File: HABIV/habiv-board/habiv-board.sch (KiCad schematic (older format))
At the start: 84 parts, among them IC1 RTC_PCF8523T, J1 Conn_01x11_Male, J10 Conn_01x02_Male, J11 Conn_02x01, J12 Conn_01x02_Male, J13 Conn_01x02_Male, J14 Conn_01x08_Male, J15 Conn_01x03_Male, J16 Conn_01x04_Male, J17 Conn_01x05_Male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

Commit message: some habiv schematic changes
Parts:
- removed J1: Conn_01x11_Male, Pin_Headers:Pin_Header_Straight_1x11_Pitch2.54mm, symbol habiv-board-rescue:Conn_01x11_Male-STM32-rescue
- added C? (x2): C_Small, symbol Device:C_Small
- added R? (x2): 8.2k, symbol Device:R_Small
- added R? (x5): 56k, symbol Device:R_Small
- added U?: LSM9DS1TR, digikey-footprints:LGA-24_3x3.5mm_LSM9DS1, symbol dk_Motion-Sensors-IMUs-Inertial-Measurement-Units:LSM9DS1TR
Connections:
- wire segments 344 -> 355
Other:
- moved on the sheet: B1, C1, C11, C12, C13, C14, C2, C8, C9, D3, D4, IC1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

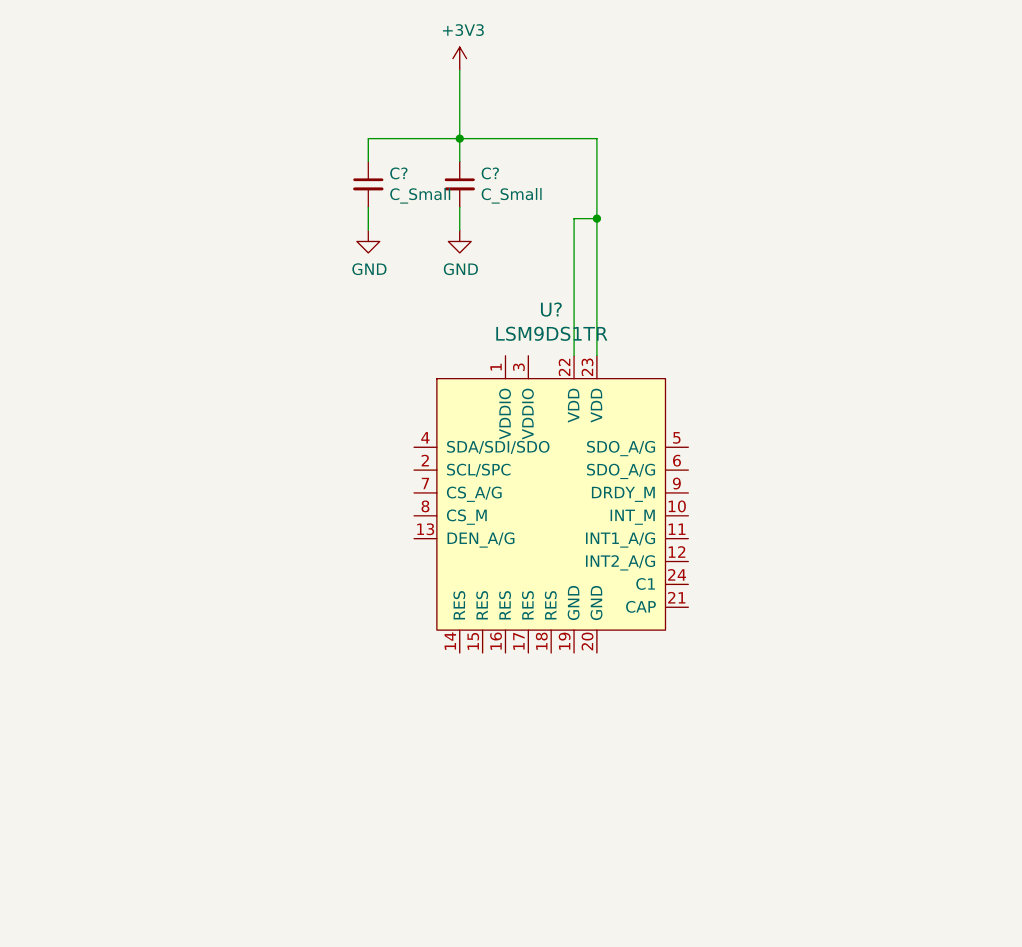
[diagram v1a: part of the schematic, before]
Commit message: implemented IMU power and ground connection with decoupling caps
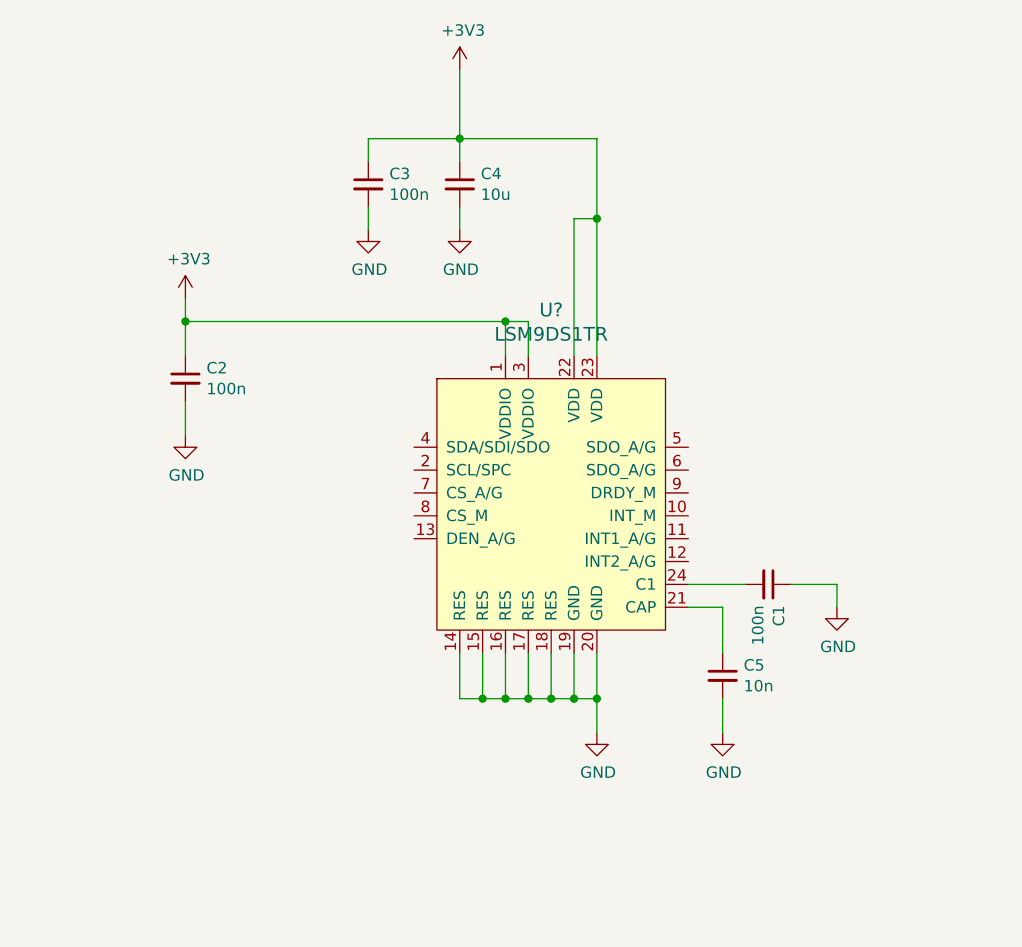
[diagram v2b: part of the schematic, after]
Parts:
- added C1, C2: 100n, symbol Device:C_Small
- added C5: 10n, symbol Device:C_Small
- C3: renamed from C?; value C_Small -> 100n
- C4: renamed from C?; value C_Small -> 10u
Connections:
- wire segments 355 -> 382
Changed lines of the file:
@@
 	17450 8750 17450 9050
 $Comp
-L Device:C_Small C?
+L Device:C_Small C4
 U 1 1 5CE00EC9
 P 17450 9250
-F 0 "C?" H 17542 9296 50  0000 L CNN
-F 1 "C_Small" H 17542 9205 50  0000 L CNN
+F 0 "C4" H 17542 9296 50  0000 L CNN
+F 1 "10u" H 17542 9205 50  0000 L CNN
 F 2 "" H 17450 9250 50  0001 C CNN
 F 3 "~" H 17450 9250 50  0001 C CNN
@@
 $EndComp
 $Comp
-L Device:C_Small C?
+L Device:C_Small C3
 U 1 1 5CEDE690
 P 17050 9250
-F 0 "C?" H 17142 9296 50  0000 L CNN
-F 1 "C_Small" H 17142 9205 50  0000 L CNN
+F 0 "C3" H 17142 9296 50  0000 L CNN
+F 1 "100n" H 17142 9205 50  0000 L CNN
 F 2 "" H 17050 9250 50  0001 C CNN
 F 3 "~" H 17050 9250 50  0001 C CNN
@@
 	1    0    0    -1
 $EndComp
+$Comp
+L Device:C_Small C5
+U 1 1 5C7D1725
+P 18600 11400
+F 0 "C5" H 18692 11446 50  0000 L CNN
+F 1 "10n" H 18692 11355 50  0000 L CNN
+F 2 "" H 18600 11400 50  0001 C CNN
+F 3 "~" H 18600 11400 50  0001 C CNN
+	1    18600 11400
+	1    0    0    -1
+$EndComp
+$Comp
+L Device:C_Small C2
+U 1 1 5C7D1829
+P 16250 10100
+F 0 "C2" H 16342 10146 50  0000 L CNN
+F 1 "100n" H 16342 10055 50  0000 L CNN
+F 2 "" H 16250 10100 50  0001 C CNN
+F 3 "~" H 16250 10100 50  0001 C CNN
+	1    16250 10100
+	1    0    0    -1
+$EndComp
+$Comp
+L Device:C_Small C1
+U 1 1 5C7D291A
+P 18800 11000
+F 0 "C1" H 18892 11046 50  0000 L CNN
+F 1 "100n" H 18892 10955 50  0000 L CNN
+F 2 "" H 18800 11000 50  0001 C CNN
+F 3 "~" H 18800 11000 50  0001 C CNN
+	1    18800 11000
+	0    1    1    0
+$EndComp
+Wire Wire Line
+	18700 11000 18450 11000
+Wire Wire Line
+	18450 11100 18600 11100
+Wire Wire Line
+	18600 11100 18600 11300
+$Comp
+L power:GND #PWR?
+U 1 1 5C85493C
+P 19100 11100
+F 0 "#PWR?" H 19100 10850 50  0001 C CNN
+F 1 "GND" H 19105 10927 50  0000 C CNN
+F 2 "" H 19100 11100 50  0001 C CNN
+F 3 "" H 19100 11100 50  0001 C CNN
+	1    19100 11100
+	1    0    0    -1
+$EndComp
+$Comp
+L power:GND #PWR?
+U 1 1 5C854A0C
+P 18600 11650
+F 0 "#PWR?" H 18600 11400 50  0001 C CNN
+F 1 "GND" H 18605 11477 50  0000 C CNN
+F 2 "" H 18600 11650 50  0001 C CNN
+F 3 "" H 18600 11650 50  0001 C CNN
+	1    18600 11650
+	1    0    0    -1
+$EndComp
+Wire Wire Line
+	18600 11500 18600 11650
+Wire Wire Line
+	19100 11100 19100 11000
+Wire Wire Line
+	19100 11000 18900 11000
+Wire Wire Line
+	17450 11300 17450 11500
+Wire Wire Line
+	17450 11500 17550 11500
+Wire Wire Line
+	17550 11500 17550 11300
+Wire Wire Line
+	17550 11500 17650 11500
+Wire Wire Line
+	17650 11500 17650 11300
+Connection ~ 17550 11500
+Wire Wire Line
+	17750 11300 17750 11500
+Wire Wire Line
+	17750 11500 17650 11500
+Connection ~ 17650 11500
+Wire Wire Line
+	17850 11300 17850 11500
+Wire Wire Line
+	17850 11500 17750 11500
+Connection ~ 17750 11500
+Wire Wire Line
+	17950 11300 17950 11500
+Wire Wire Line
+	17950 11500 17850 11500
+Connection ~ 17850 11500
+Wire Wire Line
+	18050 11300 18050 11500
+Wire Wire Line
+	18050 11500 17950 11500
+Connection ~ 17950 11500
+$Comp
+L power:GND #PWR?
+U 1 1 5C963F0A
+P 18050 11650
+F 0 "#PWR?" H 18050 11400 50  0001 C CNN
+F 1 "GND" H 18055 11477 50  0000 C CNN
+F 2 "" H 18050 11650 50  0001 C CNN
+F 3 "" H 18050 11650 50  0001 C CNN
+	1    18050 11650
+	1    0    0    -1
+$EndComp
+Wire Wire Line
+	18050 11500 18050 11650
+Connection ~ 18050 11500
+Wire Wire Line
+	17650 10000 17650 9850
+Wire Wire Line
+	17650 9850 17750 9850
+Wire Wire Line
+	17750 9850 17750 10000
+Wire Wire Line
+	17650 9850 16250 9850
+Wire Wire Line
+	16250 9850 16250 10000
+Connection ~ 17650 9850
+$Comp
+L power:GND #PWR?
+U 1 1 5C9CF645
+P 16250 10350
+F 0 "#PWR?" H 16250 10100 50  0001 C CNN
+F 1 "GND" H 16255 10177 50  0000 C CNN
+F 2 "" H 16250 10350 50  0001 C CNN
+F 3 "" H 16250 10350 50  0001 C CNN
+	1    16250 10350
+	1    0    0    -1
+$EndComp
+Wire Wire Line
+	16250 10200 16250 10350
+$Comp
+L power:+3V3 #PWR?
+U 1 1 5C9F3C2A
+P 16250 9750
+F 0 "#PWR?" H 16250 9600 50  0001 C CNN
+F 1 "+3V3" H 16265 9923 50  0000 C CNN
+F 2 "" H 16250 9750 50  0001 C CNN
+F 3 "" H 16250 9750 50  0001 C CNN
+	1    16250 9750
+	1    0    0    -1
+$EndComp
+Wire Wire Line
+	16250 9750 16250 9850
+Connection ~ 16250 9850
 $EndSCHEMATC

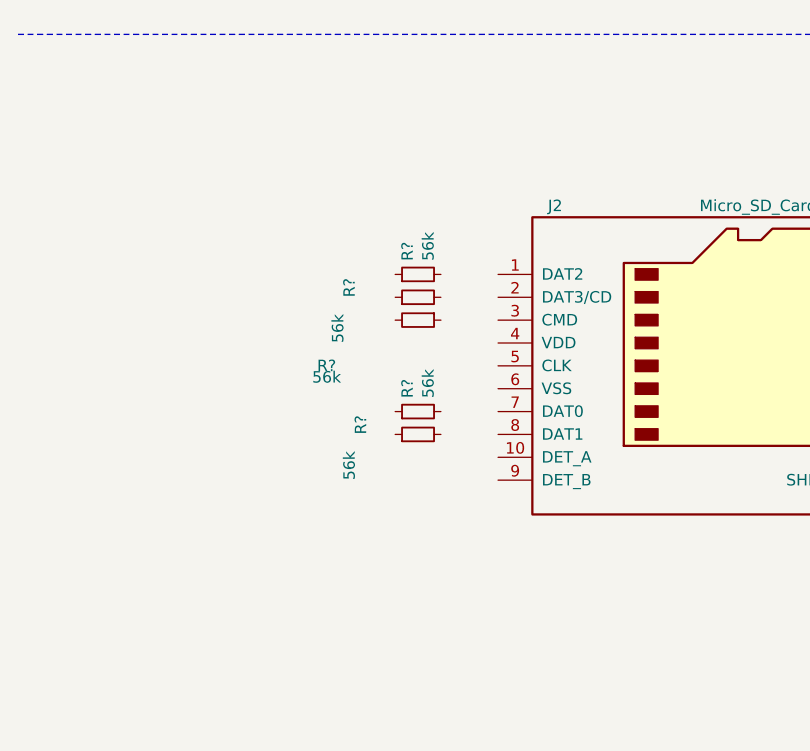
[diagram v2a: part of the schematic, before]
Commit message: SD Card connections
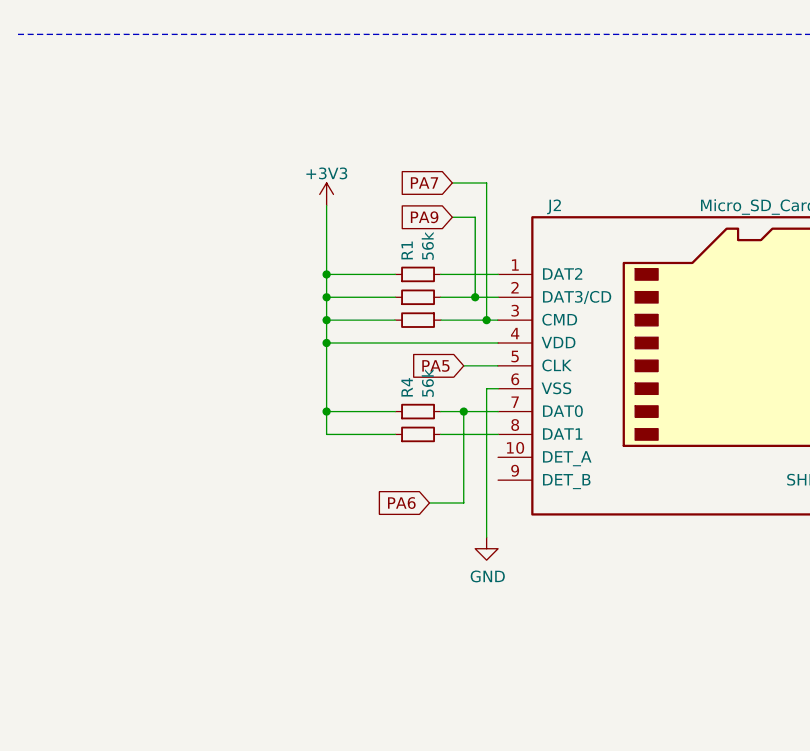
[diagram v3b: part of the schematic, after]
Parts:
- gave numbers to parts that had none: 5
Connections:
- wire segments 382 -> 411
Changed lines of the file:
@@
 	4300 15100 4300 15250
 $Comp
-L Device:R_Small R?
+L Device:R_Small R1
 U 1 1 5CBEDA09
 P 2250 14200
-F 0 "R?" H 2309 14246 50  0000 L CNN
+F 0 "R1" H 2309 14246 50  0000 L CNN
 F 1 "56k" H 2309 14155 50  0000 L CNN
 F 2 "" H 2250 14200 50  0001 C CNN
@@
 $EndComp
 $Comp
-L Device:R_Small R?
+L Device:R_Small R2
 U 1 1 5CCA87E6
 P 2250 14300
-F 0 "R?" H 2250 14600 50  0000 L CNN
-F 1 "56k" H 2050 14650 50  0000 L CNN
+F 0 "R2" H 2250 14600 50  0001 L CNN
+F 1 "56k" H 2050 14650 50  0001 L CNN
 F 2 "" H 2250 14300 50  0001 C CNN
 F 3 "~" H 2250 14300 50  0001 C CNN
@@
 $EndComp
 $Comp
-L Device:R_Small R?
+L Device:R_Small R4
 U 1 1 5CCE56CA
 P 2250 14800
-F 0 "R?" H 2309 14846 50  0000 L CNN
+F 0 "R4" H 2309 14846 50  0000 L CNN
 F 1 "56k" H 2309 14755 50  0000 L CNN
 F 2 "" H 2250 14800 50  0001 C CNN
@@
 $EndComp
 $Comp
-L Device:R_Small R?
+L Device:R_Small R5
 U 1 1 5CD03D14
 P 2250 14900
-F 0 "R?" H 2250 15150 50  0000 L CNN
-F 1 "56k" H 2050 15200 50  0000 L CNN
+F 0 "R5" H 2250 15150 50  0001 L CNN
+F 1 "56k" H 2050 15200 50  0001 L CNN
 F 2 "" H 2250 14900 50  0001 C CNN
 F 3 "~" H 2250 14900 50  0001 C CNN
@@
 $EndComp
 $Comp
-L Device:R_Small R?
+L Device:R_Small R3
 U 1 1 5CD2271E
 P 2250 14400
-F 0 "R?" V 2450 14000 50  0000 C CNN
-F 1 "56k" V 2500 14000 50  0000 C CNN
+F 0 "R3" V 2450 14000 50  0001 C CNN
+F 1 "56k" V 2500 14000 50  0001 C CNN
 F 2 "" H 2250 14400 50  0001 C CNN
 F 3 "~" H 2250 14400 50  0001 C CNN
@@
 	16250 9750 16250 9850
 Connection ~ 16250 9850
+$Comp
+L power:+3V3 #PWR?
+U 1 1 5CA19B2F
+P 1850 13900
+F 0 "#PWR?" H 1850 13750 50  0001 C CNN
+F 1 "+3V3" H 1850 14040 50  0000 C CNN
+F 2 "" H 1850 13900 50  0001 C CNN
+F 3 "" H 1850 13900 50  0001 C CNN
+	1    1850 13900
+	1    0    0    -1
+$EndComp
+Wire Wire Line
+	2150 14200 1850 14200
+Wire Wire Line
+	1850 14200 1850 13900
+Wire Wire Line
+	2350 14200 2600 14200
+Wire Wire Line
+	2350 14300 2500 14300
+Wire Wire Line
+	2150 14300 1850 14300
+Wire Wire Line
+	1850 14300 1850 14200
+Connection ~ 1850 14200
+Wire Wire Line
+	2350 14400 2550 14400
+Wire Wire Line
+	2150 14400 1850 14400
+Wire Wire Line
+	1850 14400 1850 14300
+Connection ~ 1850 14300
+Wire Wire Line
+	2600 14500 1850 14500
+Wire Wire Line
+	1850 14500 1850 14400
+Connection ~ 1850 14400
+Wire Wire Line
+	2150 14800 1850 14800
+Wire Wire Line
+	1850 14800 1850 14500
+Connection ~ 1850 14500
+Wire Wire Line
+	2350 14800 2450 14800
+Wire Wire Line
+	2150 14900 1850 14900
+Wire Wire Line
+	1850 14900 1850 14800
+Connection ~ 1850 14800
+Wire Wire Line
+	2350 14900 2600 14900
+Text GLabel 2300 15200 0    50   Input ~ 0
+PA6
+Wire Wire Line
+	2300 15200 2450 15200
+Wire Wire Line
+	2450 15200 2450 14800
+Connection ~ 2450 14800
+Wire Wire Line
+	2450 14800 2600 14800
+$Comp
+L power:GND #PWR?
+U 1 1 5CC89801
+P 2550 15350
+F 0 "#PWR?" H 2550 15100 50  0001 C CNN
+F 1 "GND" H 2555 15177 50  0000 C CNN
+F 2 "" H 2550 15350 50  0001 C CNN
+F 3 "" H 2550 15350 50  0001 C CNN
+	1    2550 15350
+	1    0    0    -1
+$EndComp
+Wire Wire Line
+	2600 14700 2550 14700
+Wire Wire Line
+	2550 14700 2550 15350
+Text GLabel 2450 14600 0    50   Input ~ 0
+PA5
+Wire Wire Line
+	2450 14600 2600 14600
+Text GLabel 2400 13950 0    50   Input ~ 0
+PA9
+Connection ~ 2500 14300
+Wire Wire Line
+	2500 14300 2600 14300
+Text GLabel 2400 13800 0    50   Input ~ 0
+PA7
+Wire Wire Line
+	2400 13800 2550 13800
+Wire Wire Line
+	2550 13800 2550 14400
+Connection ~ 2550 14400
+Wire Wire Line
+	2550 14400 2600 14400
+Wire Wire Line
+	2400 13950 2500 13950
+Wire Wire Line
+	2500 13950 2500 14300
 $EndSCHEMATC

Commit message: implemented 0 ohm resistors on Vdd pins of ICs, continue to implement 0 ohms on SPI and I2C pin
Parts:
- added R0 (x8), R? (x14): 0, symbol Device:R
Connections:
- wire segments 411 -> 424
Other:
- moved on the sheet: 100nF2, 1uF2

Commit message: finished implementing 0 ohm resistors on clock pins
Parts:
- added R? (x5): 0, symbol Device:R
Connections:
- wire segments 424 -> 427
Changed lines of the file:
@@
 	10300 2150 10400 2150
 Wire Wire Line
-	10500 2450 10500 1950
+	10500 2450 10500 2300
 Wire Wire Line
 	10500 1950 10300 1950
@@
 	12100 2800 12100 2650
 Wire Wire Line
-	10400 2150 10400 2800
+	10400 2150 10400 2250
 Wire Wire Line
 	13050 14850 12350 14850
@@
 	10300 3000 10550 3000
 Wire Wire Line
-	10300 2350 10300 3000
+	10300 2350 10300 2550
 Text GLabel 10550 3000 2    50   Input ~ 0
 PC7
@@
 Text GLabel 19100 1650 2    50   Input ~ 0
 PA8
-Wire Wire Line
-	2450 3300 2200 3300
 Wire Wire Line
 	1500 3000 1600 3000
@@
 $EndComp
 Wire Wire Line
-	1750 3250 2250 3250
-Wire Wire Line
-	2450 3200 2250 3200
-Wire Wire Line
-	2250 3200 2250 3250
+	1750 3250 2100 3250
 Wire Wire Line
 	2450 3100 2050 3100
@@
 Wire Wire Line
 	1500 2200 1500 2450
-Wire Wire Line
-	2250 3200 2100 3200
-Connection ~ 2250 3200
-Text GLabel 2100 3200 0    50   Input ~ 0
+Text GLabel 2000 3200 0    50   Input ~ 0
 PB8
-Text GLabel 2000 3400 0    50   Input ~ 0
+Text GLabel 1950 3400 0    50   Input ~ 0
 PB9
-Wire Wire Line
-	2000 3400 2200 3400
-Wire Wire Line
-	2200 3400 2200 3300
-Connection ~ 2200 3300
-Wire Wire Line
-	2200 3300 1600 3300
 $Comp
 L power:GND #PWR?
@@
 Wire Wire Line
 	2550 14250 2550 14400
+Wire Wire Line
+	2000 3200 2100 3200
+Wire Wire Line
+	2100 3200 2100 3250
+Connection ~ 2100 3200
+Wire Wire Line
+	2100 3200 2150 3200
+Wire Wire Line
+	1950 3400 2100 3400
+Wire Wire Line
+	2100 3400 2100 3300
+Connection ~ 2100 3300
+Wire Wire Line
+	2100 3300 1600 3300
+Wire Wire Line
+	2100 3300 2150 3300
+$Comp
+L Device:R R?
+U 1 1 5D6F92C2
+P 2300 3300
+F 0 "R?" H 2370 3346 50  0000 L CNN
+F 1 "0" V 2300 3250 50  0000 L CNN
+F 2 "" V 2230 3300 50  0001 C CNN
+F 3 "~" H 2300 3300 50  0001 C CNN
+	1    2300 3300
+	0    1    1    0
+$EndComp
+$Comp
+L Device:R R?
+U 1 1 5D6F9447
+P 2300 3200
+F 0 "R?" H 2370 3246 50  0000 L CNN
+F 1 "0" V 2300 3150 50  0000 L CNN
+F 2 "" V 2230 3200 50  0001 C CNN
+F 3 "~" H 2300 3200 50  0001 C CNN
+	1    2300 3200
+	0    1    1    0
+$EndComp
+$Comp
+L Device:R R?
+U 1 1 5D6FA677
+P 10500 2150
+F 0 "R?" H 10570 2196 50  0000 L CNN
+F 1 "0" V 10500 2100 50  0000 L CNN
+F 2 "" V 10430 2150 50  0001 C CNN
+F 3 "~" H 10500 2150 50  0001 C CNN
+	1    10500 2150
+	1    0    0    -1
+$EndComp
+Wire Wire Line
+	10500 2000 10500 1950
+$Comp
+L Device:R R?
+U 1 1 5D6FA78C
+P 10400 2400
+F 0 "R?" H 10470 2446 50  0000 L CNN
+F 1 "0" V 10400 2350 50  0000 L CNN
+F 2 "" V 10330 2400 50  0001 C CNN
+F 3 "~" H 10400 2400 50  0001 C CNN
+	1    10400 2400
+	1    0    0    -1
+$EndComp
+Wire Wire Line
+	10400 2550 10400 2800
+$Comp
+L Device:R R?
+U 1 1 5D6FA891
+P 10300 2700
+F 0 "R?" H 10370 2746 50  0000 L CNN
+F 1 "0" V 10300 2650 50  0000 L CNN
+F 2 "" V 10230 2700 50  0001 C CNN
+F 3 "~" H 10300 2700 50  0001 C CNN
+	1    10300 2700
+	1    0    0    -1
+$EndComp
+Wire Wire Line
+	10300 2850 10300 3000
 $EndSCHEMATC

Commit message: IMU SDA and SCL pins connected to MCU
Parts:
- added R? (x2): 0, symbol Device:R
- added R? (x2): 1K, Resistor_SMD:R_0402_1005Metric, symbol habiv-board-rescue:RESISTOR0805_NOOUTLINE-real_time_clock-eagle-import
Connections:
- wire segments 427 -> 436
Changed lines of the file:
@@
 Wire Wire Line
 	1600 3000 1750 3000
-Connection ~ 1600 3300
 Connection ~ 1750 3000
 Wire Wire Line
@@
 Wire Wire Line
 	1750 3250 2100 3250
-Wire Wire Line
-	2450 3100 2050 3100
-Wire Wire Line
-	1500 3300 1600 3300
 Wire Wire Line
 	1500 2200 2850 2200
@@
 	17750 9850 17750 10000
 Wire Wire Line
-	17650 9850 16250 9850
+	17650 9850 16900 9850
 Wire Wire Line
 	16250 9850 16250 10000
@@
 Wire Wire Line
 	10300 2850 10300 3000
+Text GLabel 16750 10500 0    50   Input ~ 0
+PB8
+Text GLabel 16750 10400 0    50   Input ~ 0
+PB9
+$Comp
+L Device:R R?
+U 1 1 5D897265
+P 17050 10400
+F 0 "R?" H 17120 10446 50  0000 L CNN
+F 1 "0" V 17050 10350 50  0000 L CNN
+F 2 "" V 16980 10400 50  0001 C CNN
+F 3 "~" H 17050 10400 50  0001 C CNN
+	1    17050 10400
+	0    1    1    0
+$EndComp
+Wire Wire Line
+	17200 10400 17250 10400
+$Comp
+L Device:R R?
+U 1 1 5D8973FE
+P 17050 10500
+F 0 "R?" H 17120 10546 50  0000 L CNN
+F 1 "0" V 17050 10450 50  0000 L CNN
+F 2 "" V 16980 10500 50  0001 C CNN
+F 3 "~" H 17050 10500 50  0001 C CNN
+	1    17050 10500
+	0    1    1    0
+$EndComp
+Wire Wire Line
+	17200 10500 17250 10500
+$Comp
+L habiv-board-rescue:RESISTOR0805_NOOUTLINE-real_time_clock-eagle-import R?
+U 1 0 5D898CF1
+P 16900 10100
+F 0 "R?" H 16900 10200 50  0000 C CNN
+F 1 "1K" H 16900 10100 40  0000 C CNB
+F 2 "Resistor_SMD:R_0402_1005Metric" H 16900 10100 50  0001 C CNN
+F 3 "" H 16900 10100 50  0001 C CNN
+	1    16900 10100
+	0    1    1    0
+$EndComp
+$Comp
+L habiv-board-rescue:RESISTOR0805_NOOUTLINE-real_time_clock-eagle-import R?
+U 1 0 5D89AC27
+P 16800 10100
+F 0 "R?" H 16800 10200 50  0000 C CNN
+F 1 "1K" H 16800 10100 40  0000 C CNB
+F 2 "Resistor_SMD:R_0402_1005Metric" H 16800 10100 50  0001 C CNN
+F 3 "" H 16800 10100 50  0001 C CNN
+	1    16800 10100
+	0    1    1    0
+$EndComp
+Wire Wire Line
+	16750 10500 16800 10500
+Wire Wire Line
+	16750 10400 16900 10400
+Wire Wire Line
+	16900 10300 16900 10400
+Connection ~ 16900 10400
+Wire Wire Line
+	16800 10300 16800 10500
+Connection ~ 16800 10500
+Wire Wire Line
+	16800 10500 16900 10500
+Wire Wire Line
+	16900 9900 16900 9850
+Connection ~ 16900 9850
+Wire Wire Line
+	16900 9850 16800 9850
+Wire Wire Line
+	16800 9900 16800 9850
+Connection ~ 16800 9850
+Wire Wire Line
+	16800 9850 16250 9850
 $EndSCHEMATC

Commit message: some small fixes to schematic
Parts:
- gave numbers to parts that had none: 26
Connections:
- net labels removed: RX, RX_3V, TX
- wire segments 436 -> 434

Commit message: remove the pin headers to clean up the schematic; added 0 ohm connection from GPS FIX to PB15
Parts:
- removed B2: CR1220, Adafruit Ultimate GPS:CR1220, symbol habiv-board-rescue:BATTERYCR1220_SMT-Adafruit_Ultimate_GPS-eagle-import
- removed D2: CUS520, Adafruit Ultimate GPS:SOD-323, symbol habiv-board-rescue:DIODESOD-323-Adafruit_Ultimate_GPS-eagle-import
- removed J18: Conn_01x04_Female, Connector:FanPinHeader_1x04_P2.54mm_Vertical, symbol Connector:Conn_01x04_Female
- removed J9: Conn_01x05_Female, Connector_PinSocket_2.54mm:PinSocket_1x05_P2.54mm_Vertical, symbol Connector:Conn_01x05_Female
- removed JP1: HEADER-1X576MIL, Connector_PinHeader_2.54mm:PinHeader_1x05_P2.54mm_Vertical, symbol habiv-board-rescue:HEADER-1X576MIL-real_time_clock-eagle-import
- removed JP2: HEADER-1X970MIL, Adafruit Ultimate GPS:1X09_ROUND_70, symbol habiv-board-rescue:HEADER-1X970MIL-Adafruit_Ultimate_GPS-eagle-import
- removed R18, R19, R20, R21: 0, symbol Device:R
- added R?: 0, symbol Device:R
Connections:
- net labels removed: CSB, ENABLE, SCL, SCLK, SDA, SDI, SDO, SQW, VIN
- wire segments 434 -> 407
- no-connect marks 0 -> 3
